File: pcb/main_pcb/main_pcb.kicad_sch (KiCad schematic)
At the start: 7 parts, among them J1 Conn_02x04_Odd_Even, J2 Conn_01x02, J3 Conn_01x02, J3 Conn_01x04

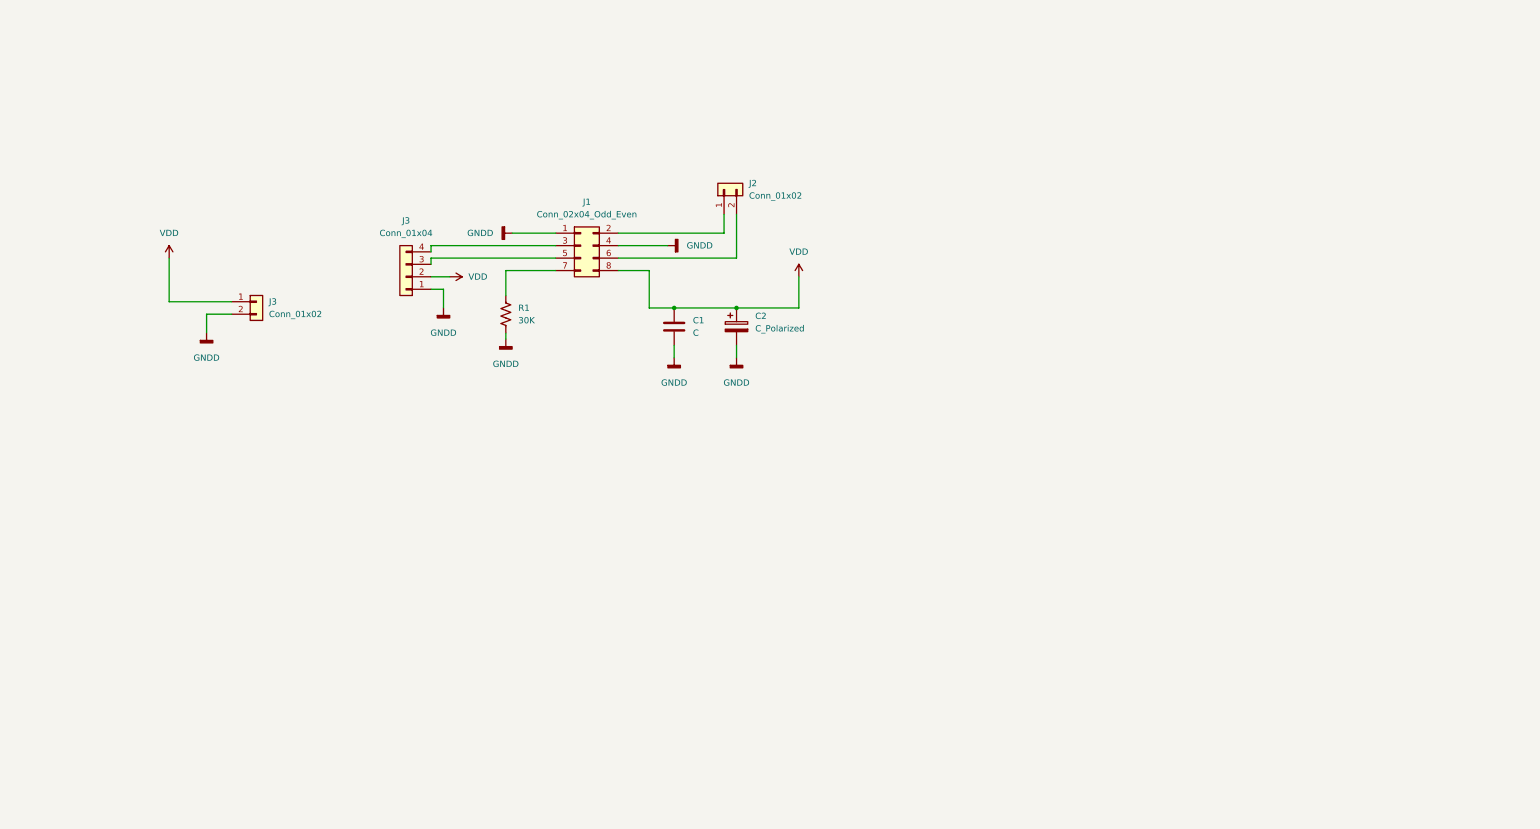
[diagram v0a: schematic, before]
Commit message: Add Teensy and motor controller to sch
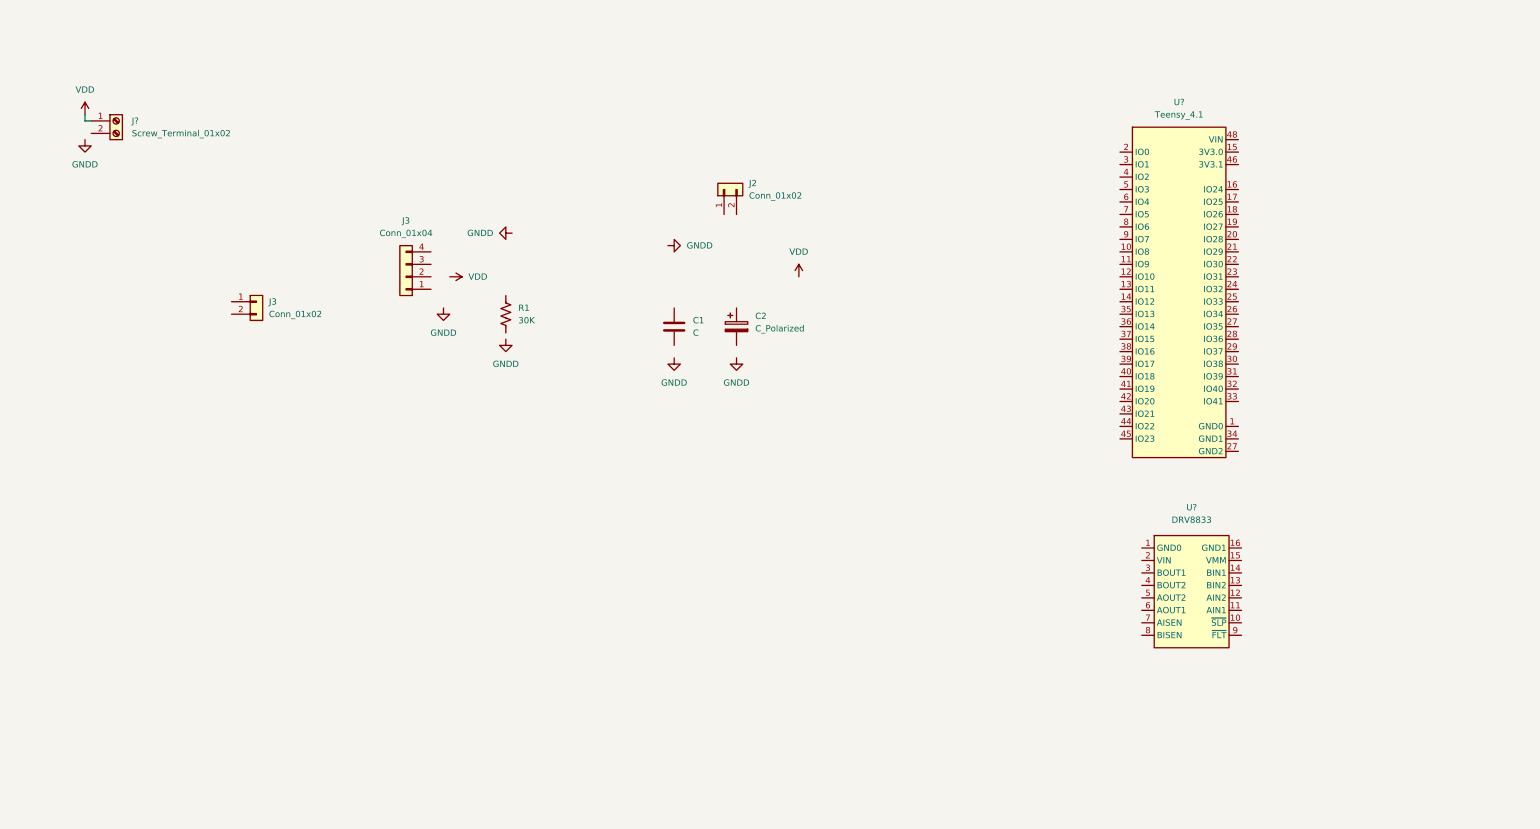
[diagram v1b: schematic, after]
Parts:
- removed J1: Conn_02x04_Odd_Even, symbol Connector_Generic:Conn_02x04_Odd_Even
- added J?: Screw_Terminal_01x02, symbol Connector:Screw_Terminal_01x02
- added U?: Teensy_4.1, symbol sym_library:Teensy_4.1
- added U?: DRV8833, symbol sym_library:DRV8833
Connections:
- net VDD: now also J?.1 (Pin_1); no longer C1.1, C2.1, J3.1 (Pin_1), J3.2 (Pin_2)
- removed net GNDD: C1.2, C2.2, J3.1 (Pin_1), J3.2 (Pin_2), R1.2

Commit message: Demonstrate Labels
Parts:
- C1: value C -> 0.1u
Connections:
- net VDD: now also J3.4 (Pin_4)
- net I2C_0: now reaches U?.16 (IO24)
- net I2C_0: now also J3.3 (Pin_3)
- net GNDD: now reaches J3.1 (Pin_1)
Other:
- moved on the sheet: C1, C2, J2, J3, R1, U?

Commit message: pcb board
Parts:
- removed C1: 0.1u, symbol Device:C
- removed C2: C_Polarized, symbol Device:C_Polarized
- removed J2, J3: Conn_01x02, symbol Connector_Generic:Conn_01x02
- removed J3: Conn_01x04, symbol Connector_Generic:Conn_01x04
- removed J?: Screw_Terminal_01x02, symbol Connector:Screw_Terminal_01x02
- removed R1: 30K, symbol Device:R_US
- removed U?: DRV8833, symbol sym_library:DRV8833
- added J? (x6): Conn_01x04, symbol Connector_Generic:Conn_01x05
- added J? (x2): Screw_Terminal_01x02, symbol Connector:Screw_Terminal_01x02
- added U?: DRV8833, symbol sym_library:DRV8833
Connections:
- net GND: now also J?.1 (Pin_1), J?.1 (Pin_1), J?.1 (Pin_1), J?.1 (Pin_1), J?.1 (Pin_1), J?.1 (Pin_1)
- net GNDPWR: now also U?.1 (GND0)
- net VDD: now also J?.5 (Pin_5), J?.5 (Pin_5), J?.5 (Pin_5), J?.5 (Pin_5), J?.5 (Pin_5), J?.5 (Pin_5)
- net at U?.10 (IO8): now also J?.4 (Pin_4)
- net at U?.11 (IO9): now also J?.4 (Pin_4)
- net at U?.12 (IO10): now also J?.4 (Pin_4)
- net at U?.13 (IO11): now also J?.4 (Pin_4)
- net at U?.14 (IO12): now also J?.4 (Pin_4)
- net at U?.17 (IO25): now also U?.12 (AIN2)
- net at U?.20 (IO28): now also U?.13 (BIN2)
- net at U?.21 (IO29): now also U?.14 (BIN1)
- net at U?.36 (IO14): now also J?.2 (Pin_2), J?.2 (Pin_2), J?.2 (Pin_2), J?.2 (Pin_2), J?.2 (Pin_2), J?.2 (Pin_2)
- net at U?.37 (IO15): now also J?.3 (Pin_3), J?.3 (Pin_3), J?.3 (Pin_3), J?.3 (Pin_3), J?.3 (Pin_3), J?.3 (Pin_3)
- net at U?.9 (IO7): now also J?.4 (Pin_4)
- net I2C_0: no longer names the net of U?.16 (IO24)
- net I2C_0: now also U?.11 (AIN1)
- new net: J?.2 (Pin_2), U?.3 (BOUT1)
- new net: J?.2 (Pin_2), U?.4 (BOUT2)
- new net: J?.1 (Pin_1), U?.5 (AOUT2)
- new net: J?.1 (Pin_1), U?.6 (AOUT1)
- new net GNDA: U?.1 (GND0), U?.16 (GND1)
- new net VDDA: U?.2 (VIN)

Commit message: Update main_pcb.kicad_sch
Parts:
- added U?: LSM6DSO, symbol sym_library:LSM6DSO
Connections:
- net GNDPWR: now also U?.27 (IO35), U?.34 (GND1)
- net at J?.2 (Pin_2), J?.2 (Pin_2), J?.2 (Pin_2)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: now also U?.9 (SDA)
- net at J?.3 (Pin_3), J?.3 (Pin_3), J?.3 (Pin_3)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: now also U?.10 (SCL)
- net at U?.40 (IO18): now also U?.7 (VIN)
- new net GNDD: U?.1 (GND), U?.8 (GND)
- no-connect marks 0 -> 46

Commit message: Update main_pcb.kicad_sch
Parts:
- added J?: Conn_01x02_Male, symbol Connector:Conn_01x02_Male
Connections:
- net GNDD: now also J?.1 (Pin_1)
- net at U?.11 (SDO): now also J?.2 (Pin_2)
- no-connect marks 46 -> 45
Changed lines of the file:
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@@
   (junction (at 179.07 130.81) (diameter 0) (color 0 0 0 0)
+  )
+  (junction (at 156.21 170.18) (diameter 0) (color 0 0 0 0)
   )
   (junction (at 177.8 64.77) (diameter 0) (color 0 0 0 0)
@@
   (no_connect (at 158.75 147.32))
   (no_connect (at 179.07 160.02))
-  (no_connect (at 179.07 157.48))
   (no_connect (at 158.75 154.94))
   (no_connect (at 158.75 157.48))
@@
   (no_connect (at 218.44 95.25))
   (no_connect (at 218.44 97.79))
+  (no_connect (at 194.31 151.13))
+  (no_connect (at 194.31 153.67))
+  (no_connect (at 194.31 148.59))
   (no_connect (at 194.31 107.95))
   (no_connect (at 194.31 105.41))
   (no_connect (at 194.31 102.87))
   (no_connect (at 194.31 100.33))
-  (no_connect (at 194.31 151.13))
-  (no_connect (at 194.31 153.67))
-  (no_connect (at 194.31 148.59))
   (wire (pts (xy 177.8 78.74) (xy 177.8 92.71))
     (stroke (width 0) (type default) (color 0 0 0 0))
@@
     (stroke (width 0) (type default) (color 0 0 0 0))
   )
+  (wire (pts (xy 185.42 176.53) (xy 156.21 176.53))
+    (stroke (width 0) (type default) (color 0 0 0 0))
+  )
   (wire (pts (xy 179.07 130.81) (xy 179.07 152.4))
     (stroke (width 0) (type default) (color 0 0 0 0))
@@
     (stroke (width 0) (type default) (color 0 0 0 0))
   )
+  (wire (pts (xy 179.07 157.48) (xy 186.69 157.48))
+    (stroke (width 0) (type default) (color 0 0 0 0))
+  )
   (wire (pts (xy 270.51 105.41) (xy 270.51 102.87))
     (stroke (width 0) (type default) (color 0 0 0 0))
@@
     (stroke (width 0) (type default) (color 0 0 0 0))
   )
+  (wire (pts (xy 156.21 176.53) (xy 156.21 170.18))
+    (stroke (width 0) (type default) (color 0 0 0 0))
+  )
   (wire (pts (xy 158.75 170.18) (xy 156.21 170.18))
     (stroke (width 0) (type default) (color 0 0 0 0))
@@
     (stroke (width 0) (type default) (color 0 0 0 0))
   )
+  (wire (pts (xy 186.69 160.02) (xy 185.42 160.02))
+    (stroke (width 0) (type default) (color 0 0 0 0))
+  )
   (wire (pts (xy 154.94 78.74) (xy 177.8 78.74))
+    (stroke (width 0) (type default) (color 0 0 0 0))
+  )
+  (wire (pts (xy 185.42 160.02) (xy 185.42 176.53))
     (stroke (width 0) (type default) (color 0 0 0 0))
   )
@@
     (pin "1")
   )
+  (symbol (lib_id "Connector:Conn_01x02_Male") (at 191.77 160.02 180) (unit 1)
+    (in_bom yes) (on_board yes) (fields_autoplaced)
+    (property "Reference" "J?" (id 0) (at 193.04 157.4799 0)
+      (effects (font (size 1.27 1.27)) (justify right) hide)
+    )
+    (property "Value" "Conn_01x02_Male" (id 1) (at 193.04 158.7499 0)
+      (effects (font (size 1.27 1.27)) (justify right) hide)
+    )
+    (property "Footprint" "" (id 2) (at 191.77 160.02 0)
+      (effects (font (size 1.27 1.27)) hide)
+    )
+    (property "Datasheet" "~" (id 3) (at 191.77 160.02 0)
+      (effects (font (size 1.27 1.27)) hide)
+    )
+    (pin "1")
+    (pin "2")
+  )
   (symbol (lib_id "power:GND") (at 154.94 48.26 90) (unit 1)
     (in_bom yes) (on_board yes)
@@
       (reference "J?") (unit 1) (value "Conn_01x04") (footprint "")
     )
+    (path "/ac784828-8dc6-4dd3-9cad-5eda6d462672"
+      (reference "J?") (unit 1) (value "Conn_01x02_Male") (footprint "")
+    )
     (path "/ba259f39-3278-4679-b3e5-fdd1b1228393"

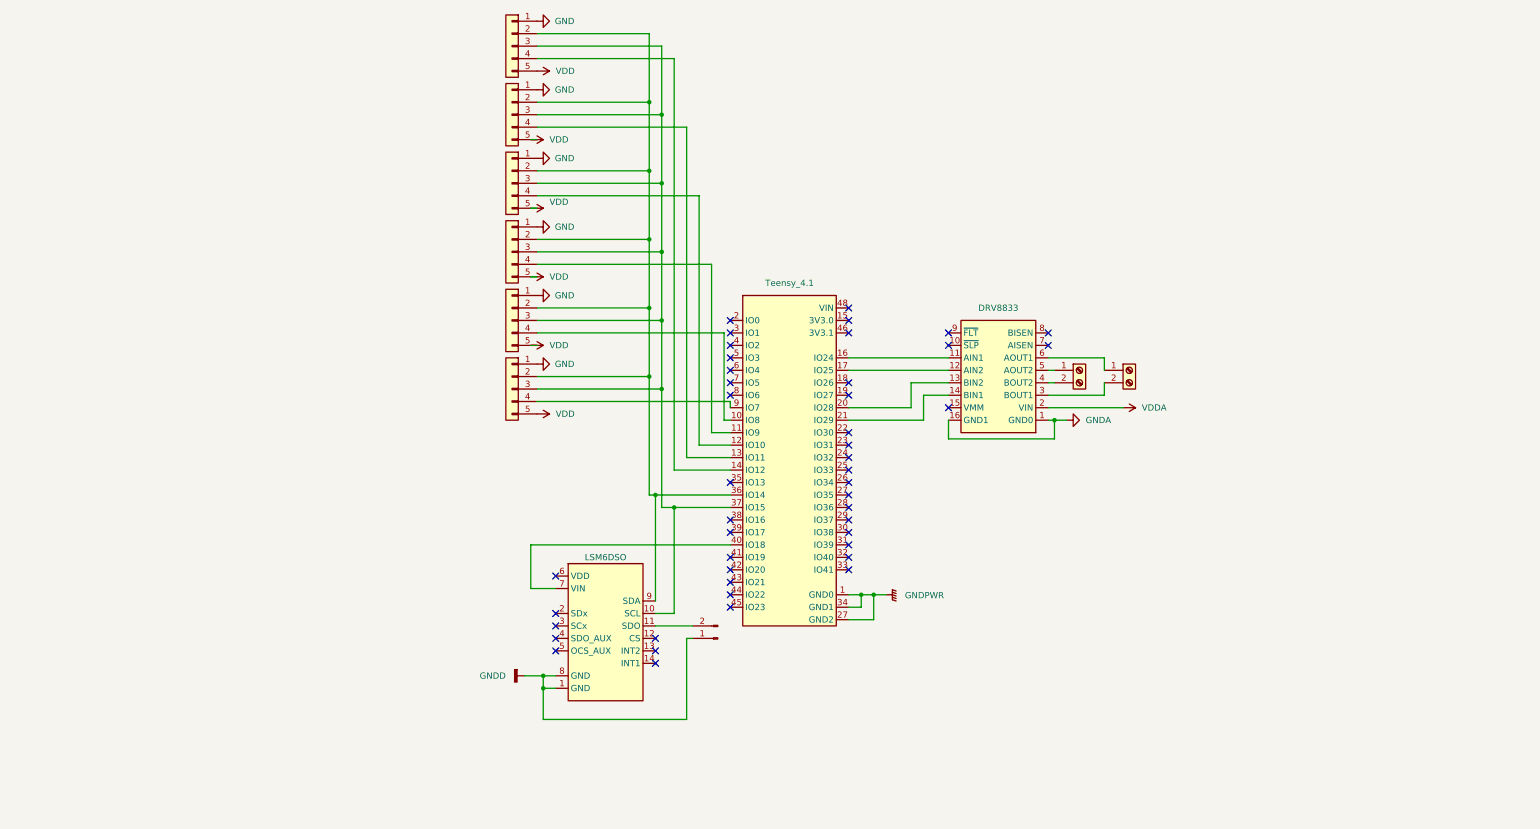
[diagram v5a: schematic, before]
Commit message: Checked pin-outs and added encoders to motor headers.
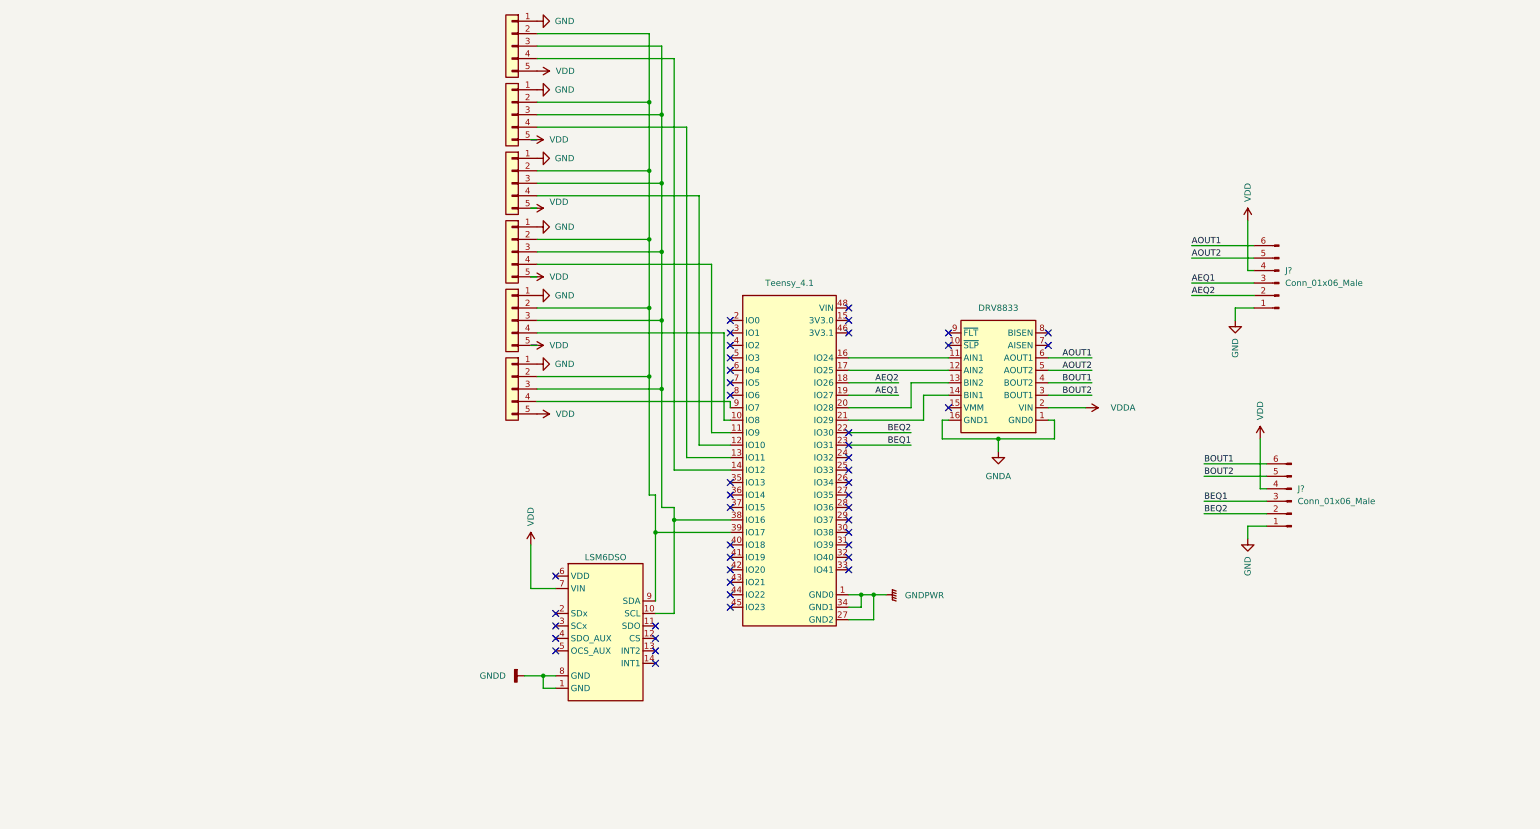
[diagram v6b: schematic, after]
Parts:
- removed J? (x2): Screw_Terminal_01x02, symbol Connector:Screw_Terminal_01x02
- removed J?: Conn_01x02_Male, symbol Connector:Conn_01x02_Male
- added J? (x2): Conn_01x06_Male, symbol Connector:Conn_01x06_Male
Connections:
- net GND: now also J?.1 (Pin_1), J?.1 (Pin_1)
- net VDD: now also U?.7 (VIN), J?.4 (Pin_4), J?.4 (Pin_4)
- net at J?.2 (Pin_2), J?.2 (Pin_2), J?.2 (Pin_2)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: now also U?.39 (IO17); no longer U?.36 (IO14)
- net at J?.3 (Pin_3), J?.3 (Pin_3), J?.3 (Pin_3)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: now also U?.38 (IO16); no longer U?.37 (IO15)
- net BOUT2: now reaches U?.3 (BOUT1)
- net BOUT2: now also J?.5 (Pin_5)
- net BOUT1: now reaches U?.4 (BOUT2)
- net BOUT1: now also J?.6 (Pin_6)
- net AOUT2: now reaches U?.5 (AOUT2)
- net AOUT2: now also J?.5 (Pin_5)
- net AOUT1: now reaches U?.6 (AOUT1)
- net AOUT1: now also J?.6 (Pin_6)
- net AEQ2: now reaches U?.18 (IO26)
- net AEQ2: now also J?.2 (Pin_2)
- net AEQ1: now reaches U?.19 (IO27)
- net AEQ1: now also J?.3 (Pin_3)
- net BEQ2: now reaches U?.22 (IO30)
- net BEQ2: now also J?.2 (Pin_2)
- net BEQ1: now reaches U?.23 (IO31)
- net BEQ1: now also J?.3 (Pin_3)
- net at U?.40 (IO18): no longer U?.7 (VIN)

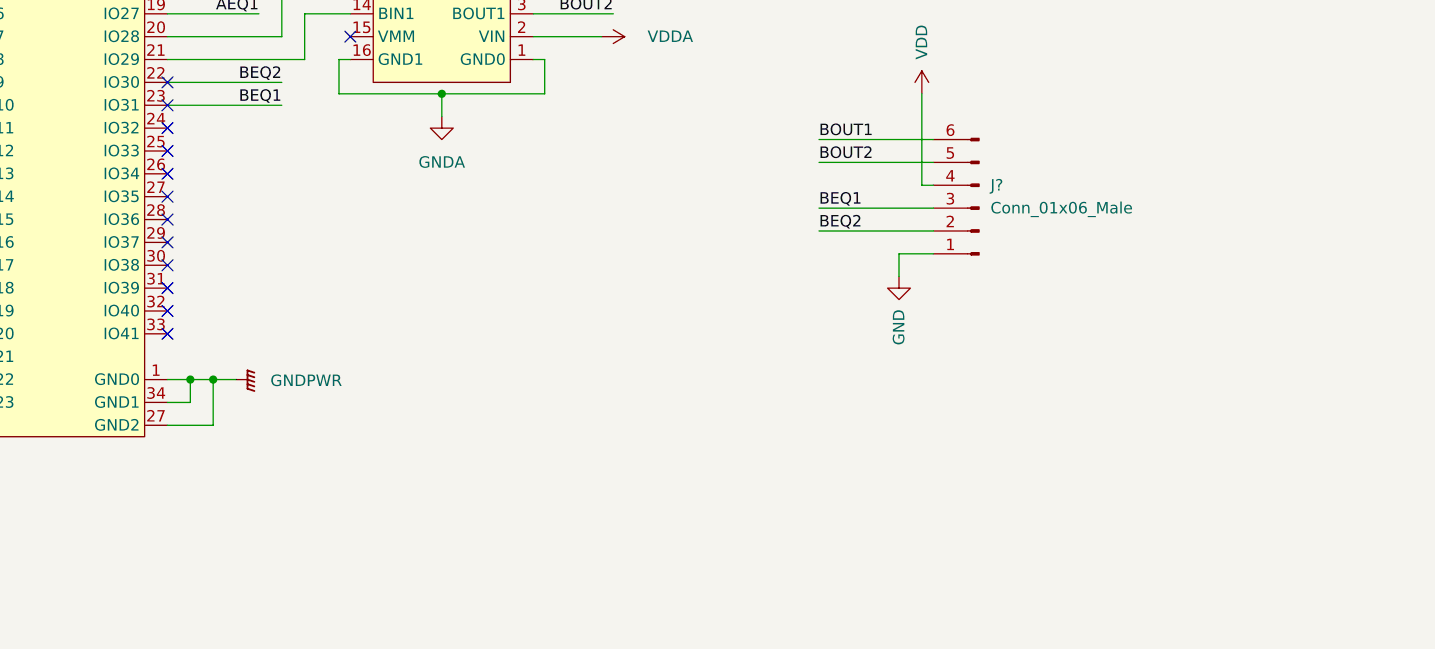
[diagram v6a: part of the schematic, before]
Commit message: Update main_pcb.kicad_sch
add ultrasonic headers
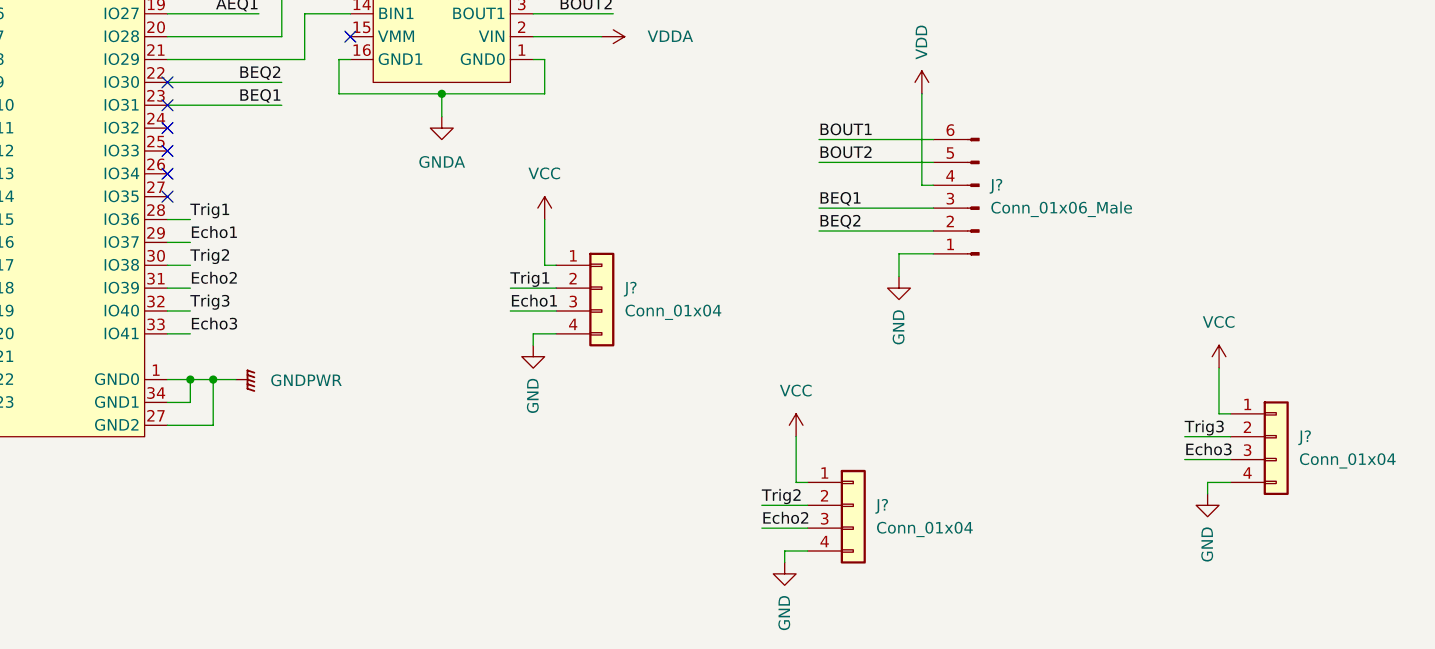
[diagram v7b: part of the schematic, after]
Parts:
- added J? (x3): Conn_01x04, symbol Connector_Generic:Conn_01x04
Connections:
- net GND: now also J?.4 (Pin_4), J?.4 (Pin_4), J?.4 (Pin_4)
- net Trig1: now reaches U?.28 (IO36)
- net Trig1: now also J?.2 (Pin_2)
- net Echo1: now reaches U?.29 (IO37)
- net Echo1: now also J?.3 (Pin_3)
- net Trig2: now reaches U?.30 (IO38)
- net Trig2: now also J?.2 (Pin_2)
- net Echo2: now reaches U?.31 (IO39)
- net Echo2: now also J?.3 (Pin_3)
- net Trig3: now reaches U?.32 (IO40)
- net Trig3: now also J?.2 (Pin_2)
- net Echo3: now reaches U?.33 (IO41)
- net Echo3: now also J?.3 (Pin_3)
- new net VCC: J?.1 (Pin_1), J?.1 (Pin_1), J?.1 (Pin_1)
- no-connect marks 45 -> 39
